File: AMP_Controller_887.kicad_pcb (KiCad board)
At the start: 2 copper layers, 79 x 61.5 mm, 65 parts, among them J1 Conn_PIC_ICSP_ICD, J3 4P_I2C, J4 Conn_01x13_Socket, J5 Conn_01x13_Socket, J6 2P_POWER, J7 USB_Mini_B_90_Angled, SW1 SW_RST, SW2 SW_PR21, X1 16MHz

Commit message: Finished layout.
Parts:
- J4, J5: footprint Connector_PinSocket_2.54mm:PinSocket_1x13_P2.54mm_Vertical -> Connector_PinSocket_2.54mm:PinSocket_1x14_P2.54mm_Vertical
- moved J7 59.2 mm to (76.8, 36.7), turned to 90 degrees
- moved C5 52.0 mm to (126.0, 33.8), turned to -90 degrees
- moved D2 49.5 mm to (71.2, 43.0), turned to 0 degrees
- moved C8 49.1 mm to (80.0, 37.8), turned to 90 degrees
- moved J1 47.0 mm to (122.7, 35.5)
- moved R3 47.0 mm to (126.0, 43.5)
- moved J6 46.8 mm to (84.0, 41.5), turned to 90 degrees
- moved R4 43.8 mm to (89.0, 63.0), turned to 90 degrees
- moved PIC16F887 38.7 mm to (91.3, 41.5), turned to 0 degrees
- moved R6 29.7 mm to (108.5, 84.5)
- moved R21 25.0 mm to (108.9, 82.0), turned to 0 degrees
- moved R7 24.0 mm to (88.0, 84.0), turned to -90 degrees
- moved C1 20.0 mm to (83.0, 70.8), turned to 90 degrees
- moved D6 18.3 mm to (117.0, 86.5), turned to -90 degrees
- moved C2 13.2 mm to (83.0, 75.8), turned to 90 degrees
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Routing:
- net /MCLR: track 0.00 -> 112.6 mm
- net VCC: track 0.00 -> 61.8 mm
- net /SCL: track 0.00 -> 57.2 mm
- net /SDA: track 0.00 -> 56.4 mm
- net /SW8: track 0.00 -> 38.1 mm
- net /AN7: track 0.00 -> 34.3 mm
- net /AN13: track 0.00 -> 32.3 mm
- net /SW6: track 0.00 -> 23.4 mm
- net /AN11: track 0.00 -> 22.8 mm
- net /SW7: track 0.00 -> 22.7 mm
- net /SW1: track 0.00 -> 20.7 mm
- net /PGD: track 0.00 -> 20.3 mm
- net /SW2: track 0.00 -> 20.2 mm
- net /SW0: track 0.00 -> 19.4 mm
- net GND: track 0.00 -> 19.2 mm, vias 0 -> 1
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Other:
- board size 79 x 61.5 mm -> 63 x 61.5 mm
- board text added: "11mm"
- board text added: "8.5mm"
- board text added: "AMP_Controller_PIC16F887 Rev.1 17th, April 2025 Made by @deulamco"
- board text added: "KiCAD"
- board text added: "Made with"
- board text added: "Mini USB-B"
- board text removed: "I2C"

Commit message: Fix power pins position to not block OLED display.
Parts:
- moved J6 48.2 mm to (79.2, 89.5)
- moved D2 16.4 mm to (87.5, 41.5), turned to 180 degrees
- moved D3 3.27 mm to (79.0, 83.2)
- moved D6 3.27 mm to (117.5, 83.2)
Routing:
- net Net-(D2-A): track 13.4 -> 53.7 mm
- net /MCLR: track 112.6 -> 107.9 mm
- net Net-(D3-A): track 6.52 -> 7.87 mm

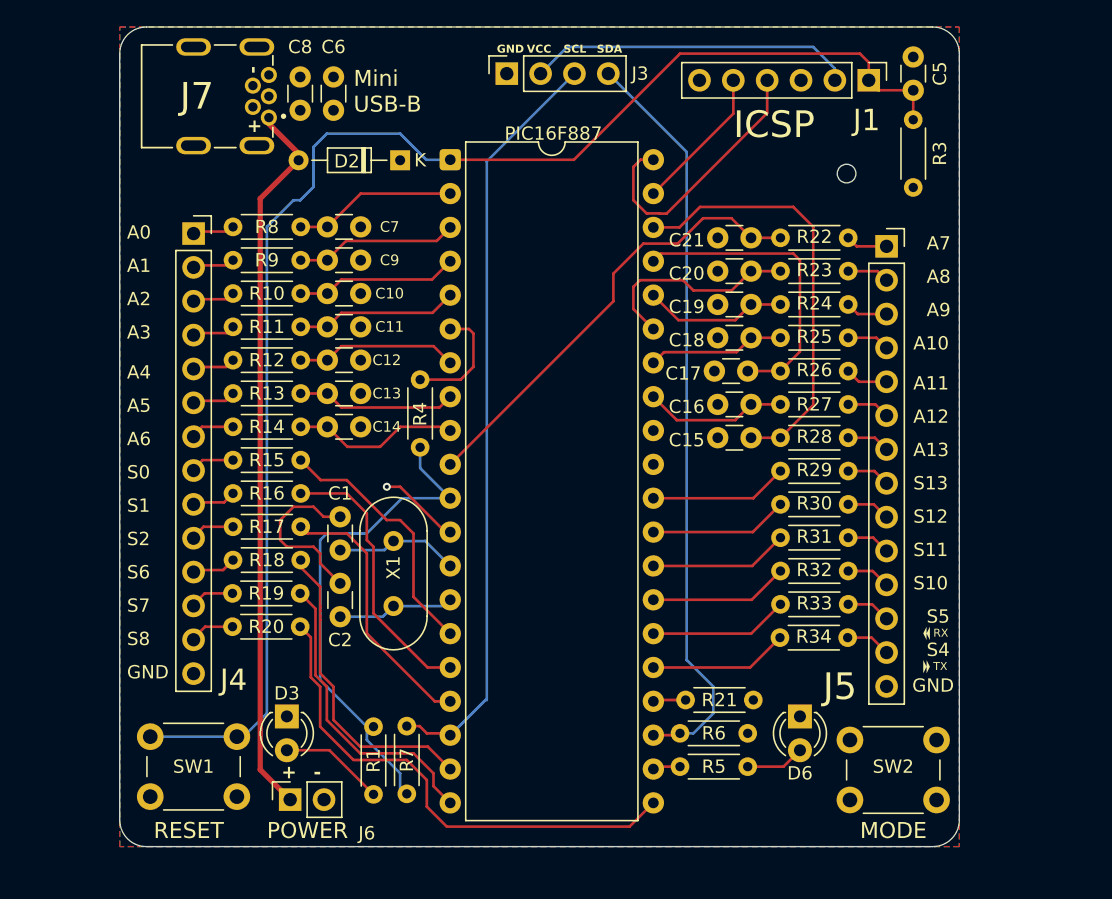
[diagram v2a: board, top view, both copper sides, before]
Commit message: Swap position of S5/S4 (aka: RX/TX) downward
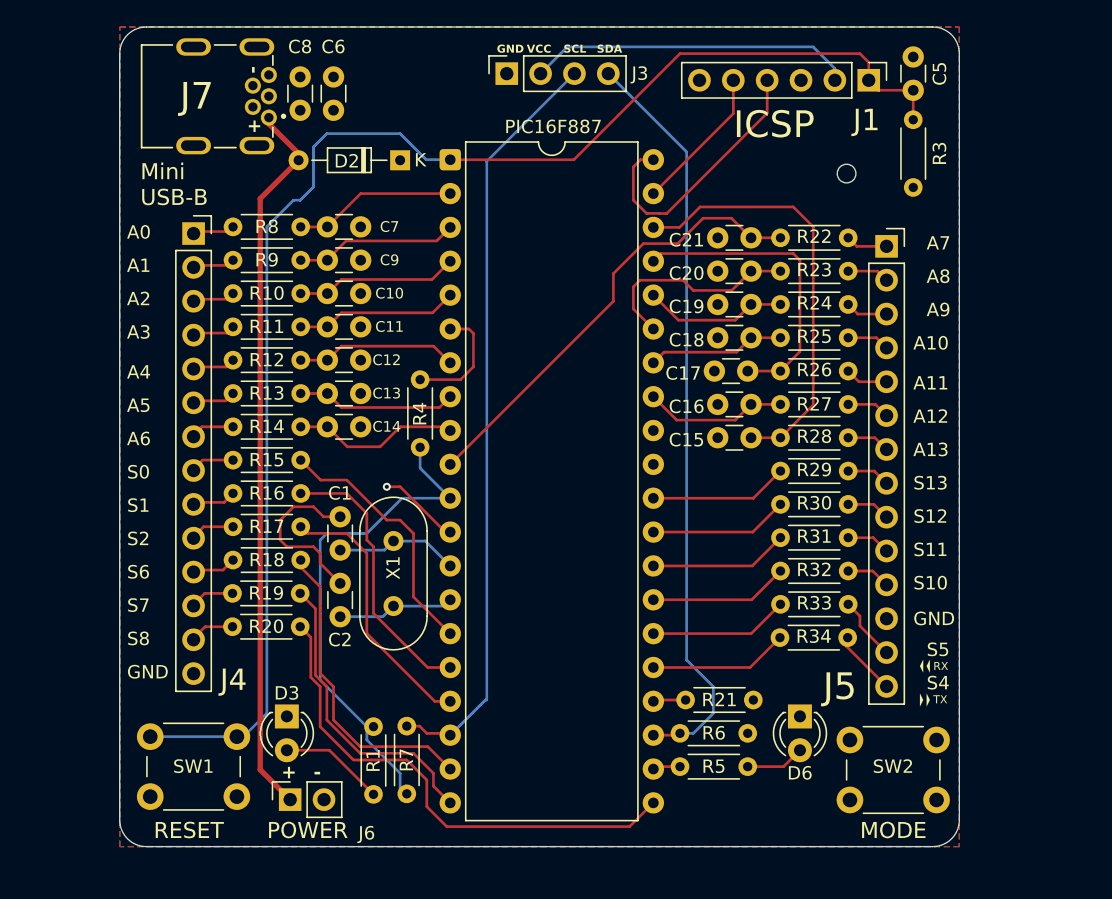
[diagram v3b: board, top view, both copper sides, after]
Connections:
- J5 pad 12: Net-(J5-Pin_12) -> GND
- J5 pad 14: GND -> Net-(J5-Pin_14)
- R33 pad 1: Net-(J5-Pin_12) -> Net-(J5-Pin_13)
- R34 pad 1: Net-(J5-Pin_13) -> Net-(J5-Pin_14)
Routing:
- net Net-(J5-Pin_14): track 0.00 -> 4.95 mm
- net Net-(J5-Pin_12): track 3.33 -> 0.00 mm
- net Net-(J5-Pin_13): track 3.38 -> 4.81 mm
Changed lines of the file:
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@@
 	(net 64 "Net-(J5-Pin_10)")
 	(net 65 "Net-(J5-Pin_11)")
-	(net 66 "Net-(J5-Pin_12)")
+	(net 66 "Net-(J5-Pin_14)")
 	(net 67 "Net-(J5-Pin_13)")
 	(net 68 "VCC")
@@
 			(layers "*.Cu" "*.Mask")
 			(remove_unused_layers no)
-			(net 66 "Net-(J5-Pin_12)")
+			(net 67 "Net-(J5-Pin_13)")
 			(pintype "passive")
 		)
@@
 			(layers "*.Cu" "*.Mask")
 			(remove_unused_layers no)
-			(net 66 "Net-(J5-Pin_12)")
+			(net 2 "GND")
 			(pinfunction "Pin_12")
 			(pintype "passive")
@@
 			(layers "*.Cu" "*.Mask")
 			(remove_unused_layers no)
-			(net 2 "GND")
+			(net 66 "Net-(J5-Pin_14)")
 			(pinfunction "Pin_14")
 			(pintype "passive")
@@
 		(tags "THT DIP DIL PDIP 2.54mm 15.24mm 600mil")
 		(property "Reference" "PIC16F887"
-			(at 7.74 -1.96 180)
+			(at 7.74 -2.46 180)
 			(layer "F.SilkS" knockout)
 			(effects
@@
 			(layers "*.Cu" "*.Mask")
 			(remove_unused_layers no)
-			(net 67 "Net-(J5-Pin_13)")
+			(net 66 "Net-(J5-Pin_14)")
 			(pintype "passive")
 		)
@@
 	(gr_poly
 		(pts
-			(xy 127.25 76.5) (xy 127 77) (xy 127.25 77.5)
+			(xy 126.75 78.96) (xy 126.5 79.46) (xy 126.75 79.96)
 		)
 		(stroke
@@
 	(gr_poly
 		(pts
-			(xy 126.75 79) (xy 127 79.5) (xy 126.75 80)
+			(xy 127.25 78.96) (xy 127 79.46) (xy 127.25 79.96)
 		)
 		(stroke
@@
 	(gr_poly
 		(pts
-			(xy 127 79) (xy 127.25 79.5) (xy 127 80)
+			(xy 127 81.5) (xy 127.25 82) (xy 127 82.5)
 		)
 		(stroke
@@
 	(gr_poly
 		(pts
-			(xy 127 76.5) (xy 126.75 77) (xy 127 77.5)
+			(xy 126.5 81.5) (xy 126.75 82) (xy 126.5 82.5)
 		)
 		(stroke
@@
 		(layer "Edge.Cuts")
 	)
-	(gr_text "S5"
-		(at 127 76.32 0)
-		(layer "F.SilkS" knockout)
-		(effects
-			(font
-				(size 1 1)
-				(thickness 0.1)
-			)
-			(justify left bottom)
-		)
-	)
 	(gr_text "A5"
 		(at 67 60.5 0)
@@
 		)
 	)
-	(gr_text "TX"
-		(at 127.5 79.82 0)
-		(layer "F.SilkS")
-		(effects
-			(font
-				(size 0.6 0.6)
-				(thickness 0.1)
-			)
-			(justify left bottom)
-		)
-	)
 	(gr_text "S10"
 		(at 126 73.82 0)
@@
 		)
 	)
-	(gr_text "Mini\nUSB-B"
-		(at 84 38 0)
+	(gr_text "Mini  \nUSB-B "
+		(at 68 45 0)
 		(layer "F.SilkS" knockout)
 		(effects
 			(font
 				(size 1.2 1.2)
-				(thickness 0.1)
+				(thickness 0.15)
 			)
 			(justify left bottom)
@@
 		)
 	)
+	(gr_text "S4"
+		(at 127 81.32 0)
+		(layer "F.SilkS" knockout)
+		(effects
+			(font
+				(size 1 1)
+				(thickness 0.1)
+			)
+			(justify left bottom)
+		)
+	)
 	(gr_text "S6"
 		(at 67 73 0)
@@
 		)
 	)
+	(gr_text "S5"
+		(at 127 78.82 0)
+		(layer "F.SilkS" knockout)
+		(effects
+			(font
+				(size 1 1)
+				(thickness 0.1)
+			)
+			(justify left bottom)
+		)
+	)
 	(gr_text "-"
 		(at 77 35 90)
@@
 		)
 	)
+	(gr_text "RX"
+		(at 127.5 79.82 0)
+		(layer "F.SilkS")
+		(effects
+			(font
+				(size 0.6 0.6)
+				(thickness 0.1)
+			)
+			(justify left bottom)
+		)
+	)
 	(gr_text "MODE"
 		(at 122 92.5 0)
@@
 		)
 	)
+	(gr_text "TX"
+		(at 127.5 82.32 0)
+		(layer "F.SilkS")
+		(effects
+			(font
+				(size 0.6 0.6)
+				(thickness 0.1)
+			)
+			(justify left bottom)
+		)
+	)
 	(gr_text "S11"
 		(at 126 71.32 0)
@@
 		)
 	)
-	(gr_text "RX"
-		(at 127.5 77.32 0)
-		(layer "F.SilkS")
-		(effects
-			(font
-				(size 0.6 0.6)
-				(thickness 0.1)
-			)
-			(justify left bottom)
-		)
-	)
 	(gr_text "A11"
 		(at 126 58.82 0)
@@
 	)
 	(gr_text "GND"
-		(at 125.92 81.5 0)
+		(at 126 76.5 0)
 		(layer "F.SilkS" knockout)
 		(effects
@@
 		)
 	)
-	(gr_text "S4"
-		(at 127 78.82 0)
-		(layer "F.SilkS" knockout)
-		(effects
-			(font
-				(size 1 1)
-				(thickness 0.1)
-			)
-			(justify left bottom)
-		)
-	)
 	(gr_text "+"
 		(at 76 39.5 0)
@@
 	)
 	(segment
-		(start 113.84 77.02)
-		(end 106.5 77.02)
+		(start 116.04 74.82)
+		(end 113.84 77.02)
 		(width 0.2)
 		(layer "F.Cu")
@@
 	)
 	(segment
-		(start 116.04 74.82)
-		(end 113.84 77.02)
+		(start 113.84 77.02)
+		(end 106.5 77.02)
 		(width 0.2)
 		(layer "F.Cu")
@@
 	)
 	(segment
-		(start 122.92 74.82)
-		(end 124 75.9)
+		(start 121 78)
+		(end 121.02 78)
 		(width 0.2)
 		(layer "F.Cu")
@@
 	)
 	(segment
-		(start 121.12 74.82)
-		(end 122.92 74.82)
+		(start 121.08 77.32)
+		(end 121 77.4)
 		(width 0.2)
 		(layer "F.Cu")
@@
 	)
 	(segment
-		(start 122.88 77.32)
+		(start 121.02 78)
+		(end 124 80.98)
+		(width 0.2)
+		(layer "F.Cu")
+		(net 66)
+	)
+	(segment
+		(start 121 77.4)
+		(end 121 78)
+		(width 0.2)
+		(layer "F.Cu")
+		(net 66)
+	)
+	(segment
+		(start 122 76.44)
 		(end 124 78.44)
 		(width 0.2)
@@
 	)
 	(segment
-		(start 121.08 77.32)
-		(end 122.88 77.32)
+		(start 122 75.7)
+		(end 122 76.44)
+		(width 0.2)
+		(layer "F.Cu")
+		(net 67)
+	)
+	(segment
+		(start 121.12 74.82)
+		(end 122 75.7)
 		(width 0.2)
 		(layer "F.Cu")

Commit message: Rev.2 : Flip USB to be normal, remove all R/C from I/O, Fix pull-up button, refine fonts.
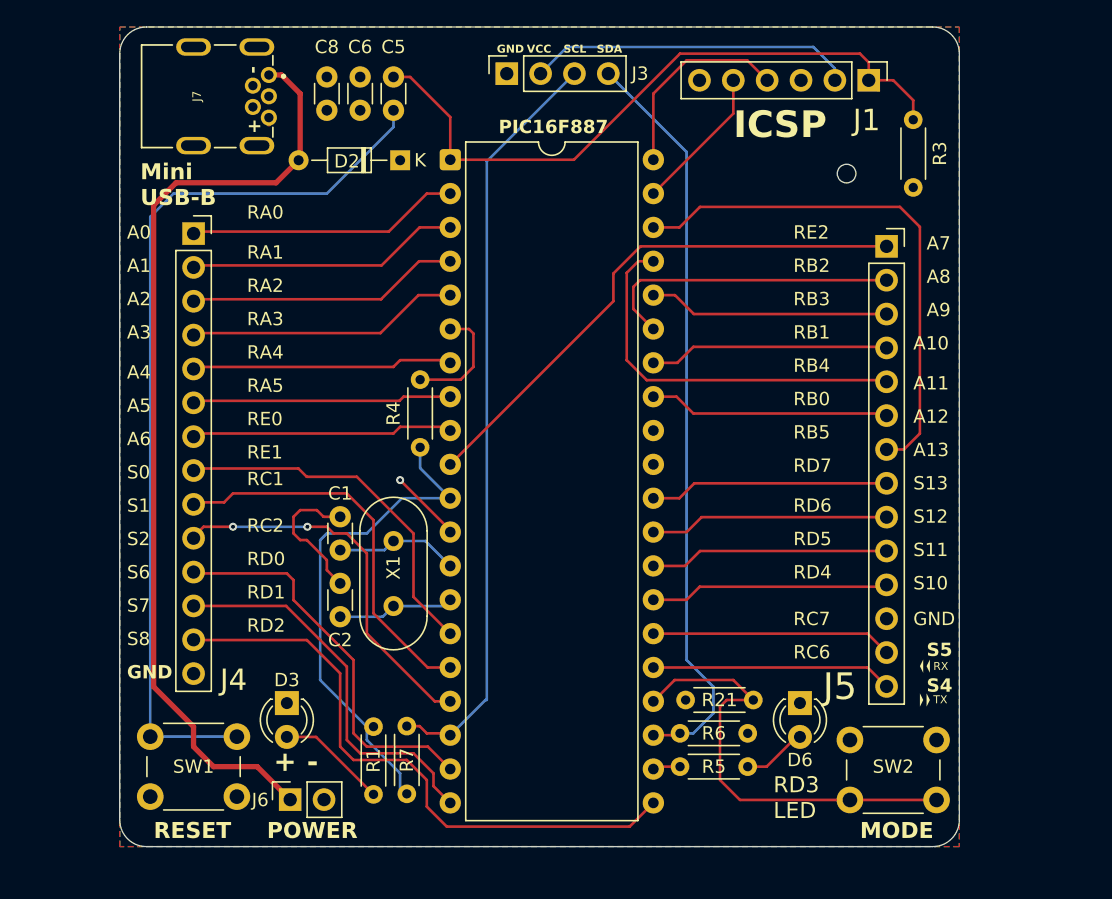
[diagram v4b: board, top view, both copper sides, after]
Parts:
- removed C10, C11, C12, C13, C14, C15, C16, C17, C18, C19, C20, C21, C7, C9: 0.1uF, Capacitor_THT:C_Disc_D3.0mm_W1.6mm_P2.50mm
- removed R10, R11, R12, R13, R14, R15, R16, R17, R18, R19, R20, R22, R23, R24, R25, R26, R27, R28, R29, R30, R31, R32, R33, R34, R8, R9: 1k, Resistor_THT:R_Axial_DIN0204_L3.6mm_D1.6mm_P5.08mm_Horizontal
- J7: footprint Connector:USB_MINI_B_90_Angled -> Connector_USB:USB_MINI_B_90_Angled
- moved C5 39.2 mm to (87.0, 37.8), turned to 90 degrees
- moved C6 2.00 mm to (84.5, 35.2)
- moved C8 2.00 mm to (82.0, 37.8)
- moved D3 1.00 mm to (79.0, 82.2)
- moved D6 1.00 mm to (117.5, 82.2)
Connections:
- C5 pad 1: GND -> Net-(C5-Pad1)
- J4 pad 1: Net-(J4-Pin_1) -> /AN0
- J4 pad 10: Net-(J4-Pin_10) -> /SW2
- J4 pad 11: Net-(J4-Pin_11) -> /SW6
- J4 pad 12: Net-(J4-Pin_12) -> /SW7
- J4 pad 13: Net-(J4-Pin_13) -> /SW8
- J4 pad 2: Net-(J4-Pin_2) -> /AN1
- J4 pad 3: Net-(J4-Pin_3) -> /AN2
- J4 pad 4: Net-(J4-Pin_4) -> /AN3
- J4 pad 5: Net-(J4-Pin_5) -> /AN4
- J4 pad 6: Net-(J4-Pin_6) -> /AN5
- J4 pad 7: Net-(J4-Pin_7) -> /AN6
- J4 pad 8: Net-(J4-Pin_8) -> /SW0
- J4 pad 9: Net-(J4-Pin_9) -> /SW1
- J5 pad 1: Net-(J5-Pin_1) -> /AN7
- J5 pad 10: Net-(J5-Pin_10) -> /SW11
- J5 pad 11: Net-(J5-Pin_11) -> /SW10
- J5 pad 13: Net-(J5-Pin_13) -> /SW5
- J5 pad 14: Net-(J5-Pin_14) -> /SW4
- J5 pad 2: Net-(J5-Pin_2) -> /AN8
- J5 pad 3: Net-(J5-Pin_3) -> /AN9
- J5 pad 4: Net-(J5-Pin_4) -> /AN10
- J5 pad 5: Net-(J5-Pin_5) -> /AN11
- J5 pad 6: Net-(J5-Pin_6) -> /AN12
- J5 pad 7: Net-(J5-Pin_7) -> /AN13
- J5 pad 8: Net-(J5-Pin_8) -> /SW13
- J5 pad 9: Net-(J5-Pin_9) -> /SW12
- J7 pad 1: GND -> Net-(D2-A)
- J7 pad 5: Net-(D2-A) -> GND
- R21 pad 1: Net-(PIC16F887-SDO/RC5) -> VCC
- R21 pad 2: VCC -> Net-(PIC16F887-SDO/RC5)
- SW1 pad 1: /MCLR -> Net-(C5-Pad1)
- SW2 pad 2: VCC -> Net-(PIC16F887-SDO/RC5)
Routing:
- net Net-(C5-Pad1): track 0.00 -> 67.8 mm
- net /MCLR: track 107.9 -> 52.0 mm
- net Net-(PIC16F887-SDO/RC5): track 2.46 -> 33.9 mm
- net Net-(D2-A): track 53.7 -> 71.0 mm
- net /SW2: track 20.2 -> 28.5 mm, vias 0 -> 2
- net /SW1: track 20.7 -> 29.0 mm
- net /AN3: track 12.2 -> 20.4 mm
- net /AN2: track 12.2 -> 20.4 mm
- net /AN0: track 12.3 -> 20.4 mm
- net /AN1: track 12.3 -> 20.4 mm
- net /AN5: track 12.0 -> 19.8 mm
- net /SW0: track 19.4 -> 27.1 mm
- net /AN10: track 10.3 -> 18.0 mm
- net /SW4: track 10.4 -> 18.1 mm
- net /SW5: track 10.5 -> 18.1 mm
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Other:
- board text added: "AMP_Controller_PIC16F887 Rev.2 30th, April 2025 Made by @deulamco"
- board text added: "RA0"
- board text added: "RA1"
- board text added: "RA2"
- board text added: "RA3"
- board text added: "RA4"
- board text added: "RA5"
- board text added: "RB0"
- board text added: "RB1"
- board text added: "RB2"
- board text added: "RB3"
- board text added: "RB4"
- board text added: "RB5"
- board text added: "RC1"
- board text added: "RC2"
- board text added: "RC6"
- board text added: "RC7"
- board text added: "RD0"
- board text added: "RD1"
- board text added: "RD2"
- board text added: "RD3 LED"
- board text added: "RD4"
- board text added: "RD5"
- board text added: "RD6"
- board text added: "RD7"
- board text added: "RE0"
- board text added: "RE1"
- board text added: "RE2"
- board text removed: "AMP_Controller_PIC16F887 Rev.1 17th, April 2025 Made by @deulamco"
